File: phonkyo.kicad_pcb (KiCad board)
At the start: 2 copper layers, 65 x 30 mm, 31 parts, among them J1 GPIO, J2 LineOutJack, J4 RIJack, U2 PCM5102A, U3 XC6206P332MR

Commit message: add: C14, 100 nF decoupling on DAC AVDD (pin 8)
AVDD (U2 pin 8) had no local decoupling. It was fed from beside pin 1
through a via and a B.Cu detour, about 9 mm from any capacitor. TI's
reference layout decouples CPVDD (pin 1) and AVDD (pin 8) separately.

C14 is a 100 nF 0402 at (146.2, 90.6), about 1.6 mm from pin 8. Its GNDA
pad sits in the analog pour. In the schematic it is the third cap on the
LDO output rails, beside C7 and C8, with its own junctions.

U2 pad 9 (AGND) is switched to a solid zone connection. Pin 9 is
wedged between pins 8 and 10, so it can only take thermal spokes to the
left and right. Decoupling pin 8 from the left necessarily uses its
left spoke, which left 1 spoke and a DRC starved-thermal error. A solid
connection is normal for a reflowed ground pin and gives AGND a
lower-impedance path. This is a per-pad override; no other pad changes.

Verified: ERC shows no new errors, and C14's nets are confirmed from
the exported netlist (pin 1 GNDA, pin 2 +3.3VA). DRC with schematic
parity: 0 unconnected, 0 parity errors, no new violations. Semantic
diff: C14 added, no other footprint moved, 2 new +3.3VA tracks, and the
pad 9 override.

Co-Authored-By: Claude Opus 5.5 <noreply@anthropic.com>
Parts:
- added C14: 0.1u, Capacitor_SMD:C_0402_1005Metric, F.Cu at (146.2, 90.6)
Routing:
- net +3.3VA: track 20.0 -> 21.8 mm

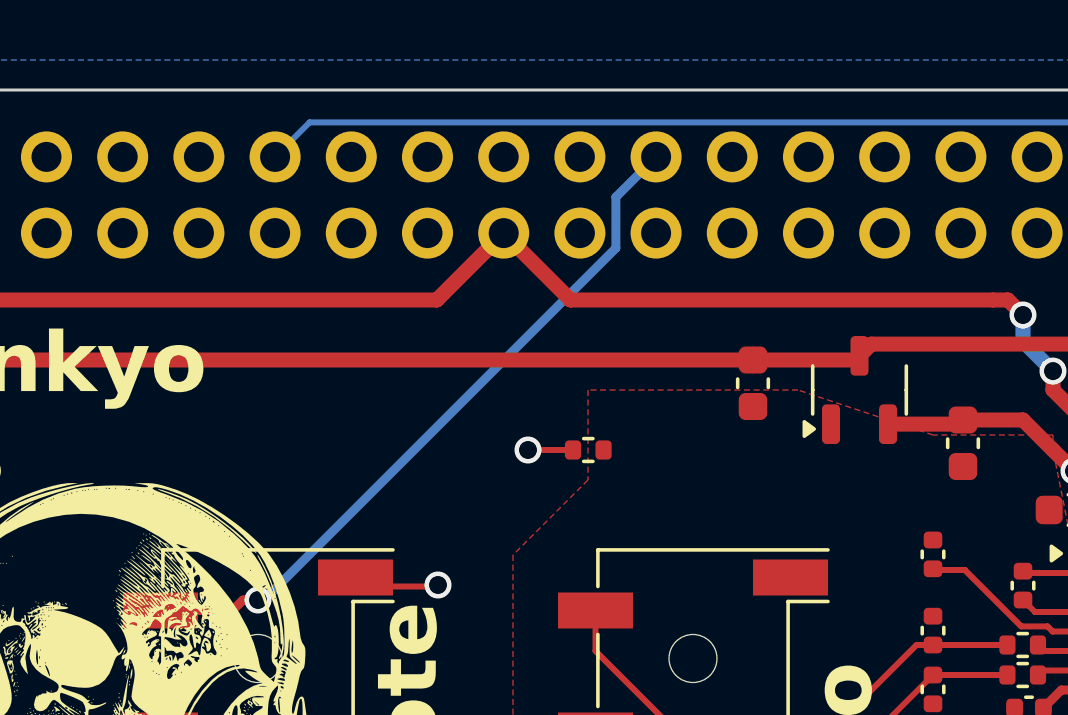
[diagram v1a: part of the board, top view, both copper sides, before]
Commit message: add: HAT ID EEPROM (CAT24C256) with pull-ups, decoupling and WP jumper
Enables the previously DNP ID EEPROM circuit so the Pi can identify the
board and load its overlay at boot:

- U1 CAT24C256, TSSOP-8, in the strip above the 3.5 mm jacks
- R1/R2 3.9k pull-ups on ID_SD/ID_SC (HAT spec value), 0402
- C1 100 nF at VCC (pin 8), with its own GND via
- JP1 solder jumper on the bottom side: open = WP floats low
  (writable, for flashing), bridged = WP tied to +3V3 (protected)

Routing is by hand. Both ID lines stay on F.Cu from the header: ID_SC
along the board edge above the header, ID_SD between the header rows.
B.Cu is used only for short vertical hops under the +3V3/+5V rails,
plus a +3V3 hop from the rail. The existing GPIO25 route is untouched.
The B.Cu GND pour stays a single piece (1733 -> 1715 mm2).

DRC with schematic parity: 0 unconnected, 0 parity, no errors; only
library-mismatch warnings, where C1/R1/R2 inherit them from the existing
0402 footprints they were cloned from. ERC is unchanged. No
pre-existing track, via or footprint is moved.

Co-Authored-By: Claude Opus 5.5 <noreply@anthropic.com>
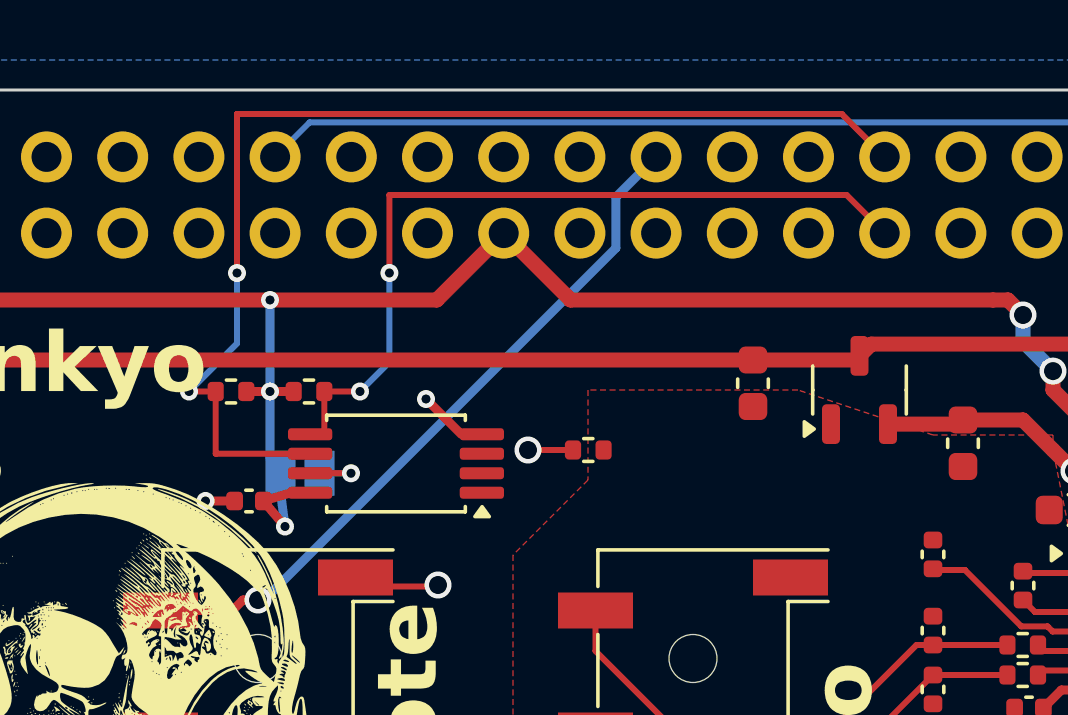
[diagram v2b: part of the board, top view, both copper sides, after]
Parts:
- added C1: 100n, Capacitor_SMD:C_0402_1005Metric, F.Cu at (120.2, 83.7)
- added JP1: ID_WP, Jumper:SolderJumper-2_P1.3mm_Open_Pad1.0x1.5mm, B.Cu at (121.9, 82.8)
- added R1: 3.9k, Resistor_SMD:R_0402_1005Metric, F.Cu at (122.2, 80.0)
- added R2: 3.9k, Resistor_SMD:R_0402_1005Metric, F.Cu at (119.6, 80.0)
- added U1: CAT24C256, Package_SO:TSSOP-8_4.4x3mm_P0.65mm, F.Cu at (125.1, 82.5)
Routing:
- net /ID_SCL: track 0.00 -> 37.6 mm, vias 0 -> 2
- net /ID_SDA: track 0.00 -> 26.6 mm, vias 0 -> 2
- net +3V3: track 54.3 -> 64.4 mm, vias 2 -> 5
- net GND: track 29.8 -> 32.4 mm, vias 10 -> 12
- net Net-(JP1-A): track 0.00 -> 1.75 mm, vias 0 -> 1
